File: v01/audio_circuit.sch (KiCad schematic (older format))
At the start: 44 parts

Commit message: ERC.
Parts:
- gave numbers to parts that had none: 44
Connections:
- net +3.3V renamed 3.3V
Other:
- note added: "+HI SPKR L"
- note added: "+HI SPKR R"
- note added: "-HI SPKR L"
- note added: "-HI SPKR R"
- note added: "I had to change VSS from being a power input (power output or passive works)\nbecause ground is a power input attached to a power output (power flag), the\n capacitor is purely passive, but the output from the power flag is not being \ndetected by the indirectly connected capacitor pin, hence the VSS input pin \nwasn't being "driven". Alternate solution besides the one listed above \nwould be to 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"

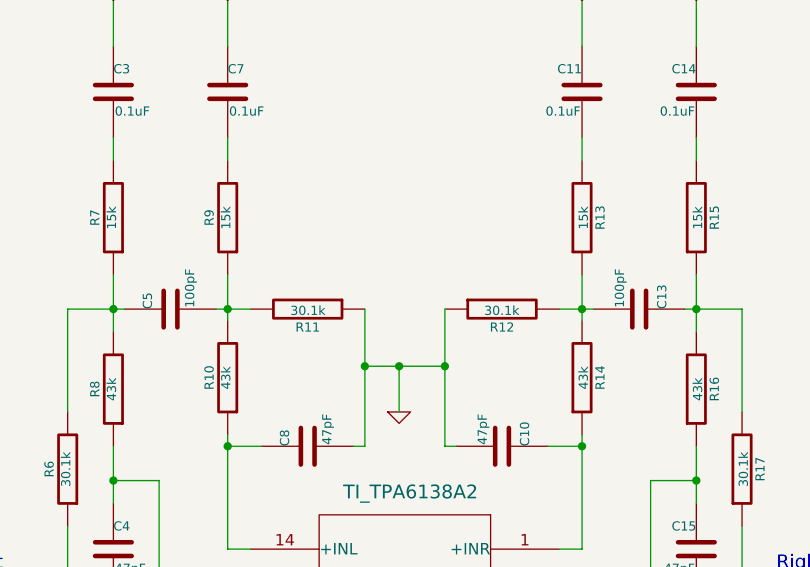
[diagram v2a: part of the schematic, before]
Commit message: updates:
1) added DIP-1 switch to connect/disconnect battery
2) annotated components in the entire schematic
3) generated netlist for the schematic
4) matched components with footprints (caps, DIP switch, diodes, LEDs, I think that's it ...)
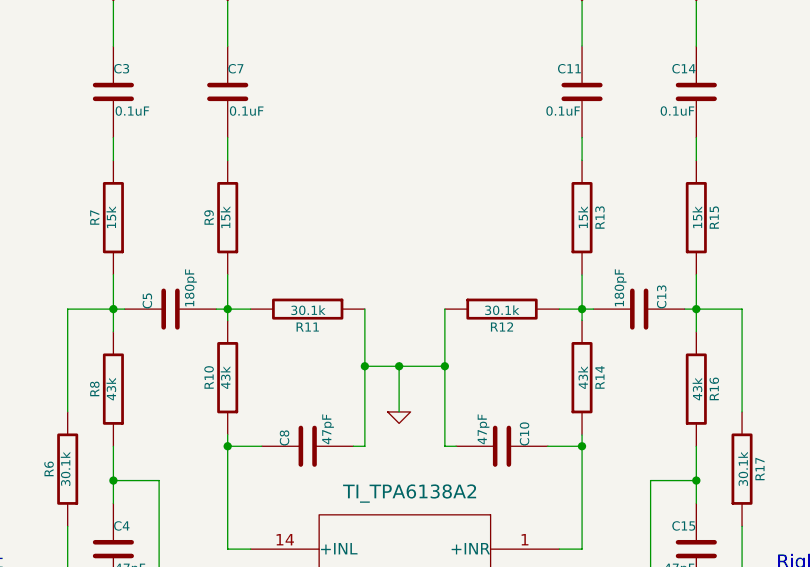
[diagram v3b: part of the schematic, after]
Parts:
- C13, C5: value 100pF -> 180pF
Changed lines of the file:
@@
 LIBS:BC127
 LIBS:mic5219
+LIBS:ab2_usb
 LIBS:CWIEM_PCB_v01-cache
 EELAYER 27 0
@@
 P 4800 3650
 F 0 "C5" H 4800 3750 40  0000 L CNN
-F 1 "100pF" H 4806 3565 40  0000 L CNN
+F 1 "180pF" H 4806 3565 40  0000 L CNN
 F 2 "~" H 4838 3500 30  0000 C CNN
 F 3 "~" H 4800 3650 60  0000 C CNN
@@
 P 6850 3650
 F 0 "C13" H 6850 3750 40  0000 L CNN
-F 1 "100pF" H 6856 3565 40  0000 L CNN
+F 1 "180pF" H 6856 3565 40  0000 L CNN
 F 2 "~" H 6888 3500 30  0000 C CNN
 F 3 "~" H 6850 3650 60  0000 C CNN
